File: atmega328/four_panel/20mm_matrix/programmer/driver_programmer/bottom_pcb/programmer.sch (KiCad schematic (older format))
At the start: 6 parts, among them P1 CONN_2, P2 CONN_3X2, P3 CONN_3X2, P4 CONN_3X2, P5 CONN_2, P6 CONN_3X2

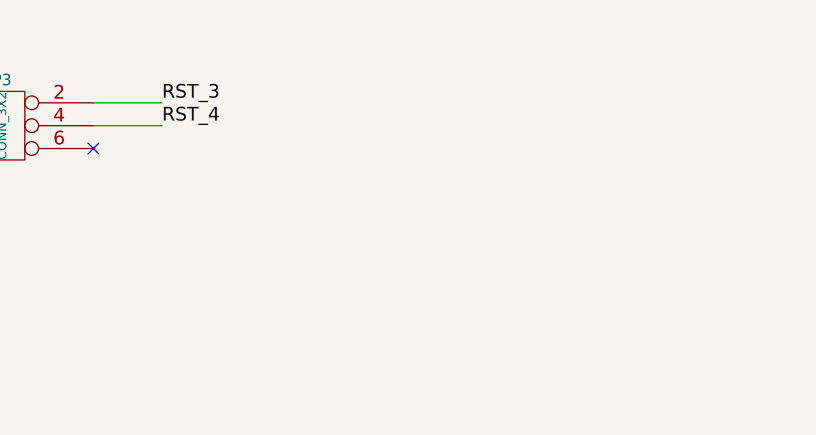
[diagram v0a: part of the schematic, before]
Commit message: Created gerber files for test_arena and programmer pcbs. Fixed of few small errors.
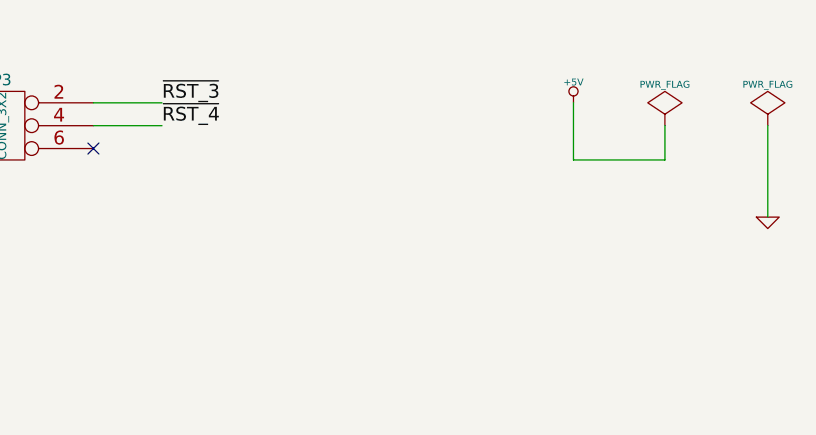
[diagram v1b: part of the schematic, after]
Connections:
- net RST_3 is gone; now on net ~RST_3: P3.2
- net RST_4 is gone; now on net ~RST_4: P3.4
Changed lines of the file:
@@
 LIBS:contrib
 LIBS:valves
+LIBS:programmer-cache
 EELAYER 24 0
 EELAYER END
@@
 NoConn ~ 6150 1300
 Text Label 7250 1100 0    60   ~ 0
-RST_3
+~RST_3
 Text Label 7250 1200 0    60   ~ 0
-RST_4
+~RST_4
 $Comp
 L CONN_2 P1
@@
 	4600 2700 4600 2400
 $Comp
-L +5V #PWR?
+L +5V #PWR07
 U 1 1 524138C0
 P 4600 2400
-F 0 "#PWR?" H 4600 2490 20  0001 C CNN
+F 0 "#PWR07" H 4600 2490 20  0001 C CNN
 F 1 "+5V" H 4600 2490 30  0000 C CNN
 F 2 "" H 4600 2400 60  0000 C CNN
@@
 	7100 2900 7100 3100
 $Comp
-L GND #PWR?
+L GND #PWR08
 U 1 1 52413904
 P 7100 3100
-F 0 "#PWR?" H 7100 3100 30  0001 C CNN
+F 0 "#PWR08" H 7100 3100 30  0001 C CNN
 F 1 "GND" H 7100 3030 30  0001 C CNN
 F 2 "" H 7100 3100 60  0000 C CNN
@@
 Text Notes 5550 3200 2    60   ~ 0
 I2C
+$Comp
+L +5V #PWR09
+U 1 1 5282D71D
+P 9050 1100
+F 0 "#PWR09" H 9050 1190 20  0001 C CNN
+F 1 "+5V" H 9050 1190 30  0000 C CNN
+F 2 "" H 9050 1100 60  0000 C CNN
+F 3 "" H 9050 1100 60  0000 C CNN
+	1    9050 1100
+	1    0    0    -1
+$EndComp
+$Comp
+L GND #PWR010
+U 1 1 5282D72C
+P 9900 1600
+F 0 "#PWR010" H 9900 1600 30  0001 C CNN
+F 1 "GND" H 9900 1530 30  0001 C CNN
+F 2 "" H 9900 1600 60  0000 C CNN
+F 3 "" H 9900 1600 60  0000 C CNN
+	1    9900 1600
+	1    0    0    -1
+$EndComp
+$Comp
+L PWR_FLAG #FLG011
+U 1 1 5282D73B
+P 9450 1200
+F 0 "#FLG011" H 9450 1295 30  0001 C CNN
+F 1 "PWR_FLAG" H 9450 1380 30  0000 C CNN
+F 2 "" H 9450 1200 60  0000 C CNN
+F 3 "" H 9450 1200 60  0000 C CNN
+	1    9450 1200
+	1    0    0    -1
+$EndComp
+$Comp
+L PWR_FLAG #FLG012
+U 1 1 5282D74A
+P 9900 1200
+F 0 "#FLG012" H 9900 1295 30  0001 C CNN
+F 1 "PWR_FLAG" H 9900 1380 30  0000 C CNN
+F 2 "" H 9900 1200 60  0000 C CNN
+F 3 "" H 9900 1200 60  0000 C CNN
+	1    9900 1200
+	1    0    0    -1
+$EndComp
+Wire Wire Line
+	9050 1100 9050 1350
+Wire Wire Line
+	9050 1350 9450 1350
+Wire Wire Line
+	9450 1350 9450 1200
+Wire Wire Line
+	9900 1200 9900 1600
 $EndSCHEMATC
